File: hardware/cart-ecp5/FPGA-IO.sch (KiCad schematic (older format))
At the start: 9 parts, among them J1 JTAG, U1 LFE5U-25F-xBG256x, U2 W25Q512JVEIM, X1 XO_Generic_NC

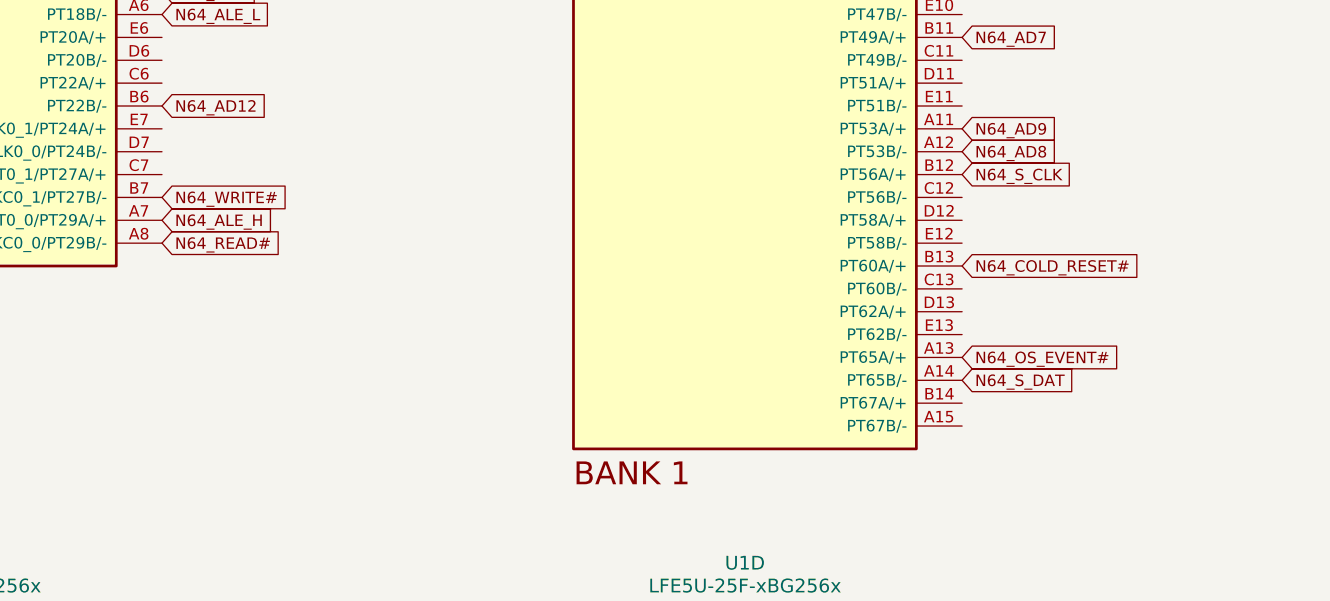
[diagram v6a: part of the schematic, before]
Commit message: Fanout MicroSD and N64 interfaces on the top layer
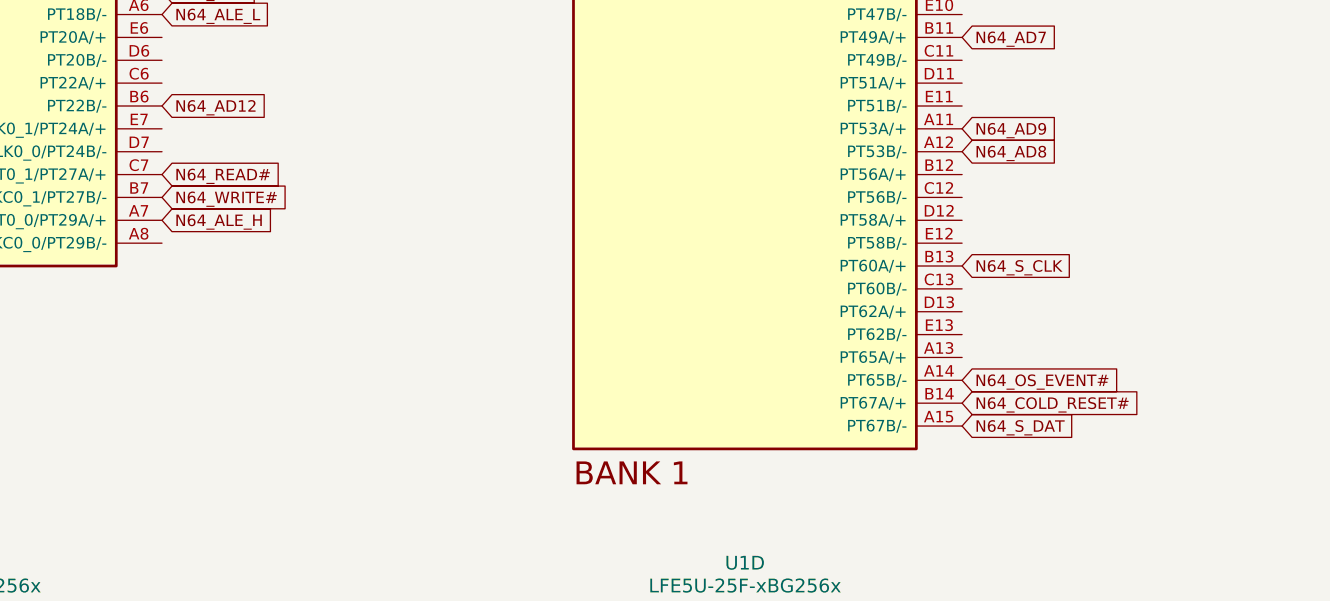
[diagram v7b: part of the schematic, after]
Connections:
- net N64_COLD_RESET#: now also U1.B14 (PT67A/+); no longer U1.B13 (PT60A/+)
- net N64_OS_EVENT#: now also U1.A14 (PT65B/-); no longer U1.A13 (PT65A/+)
- net N64_READ#: now also U1.C7 (PCLKT0_1/PT27A/+); no longer U1.A8 (PCLKC0_0/PT29B/-)
- net N64_S_CLK: now also U1.B13 (PT60A/+); no longer U1.B12 (PT56A/+)
- net N64_S_DAT: now also U1.A15 (PT67B/-); no longer U1.A14 (PT65B/-)
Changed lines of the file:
@@
 Text GLabel 3200 3800 2    50   Input ~ 0
 N64_ALE_H
-Text GLabel 3200 3900 2    50   Input ~ 0
+Text GLabel 3200 3600 2    50   Input ~ 0
 N64_READ#
 Text GLabel 6700 2600 2    50   Input ~ 0
@@
 Text GLabel 6700 3500 2    50   Input ~ 0
 N64_AD8
-Text GLabel 6700 3600 2    50   Input ~ 0
+Text GLabel 6700 4000 2    50   Input ~ 0
 N64_S_CLK
-Text GLabel 6700 4400 2    50   Input ~ 0
+Text GLabel 6700 4500 2    50   Input ~ 0
 N64_OS_EVENT#
-Text GLabel 6700 4000 2    50   Input ~ 0
+Text GLabel 6700 4600 2    50   Input ~ 0
 N64_COLD_RESET#
-Text GLabel 6700 4500 2    50   Input ~ 0
+Text GLabel 6700 4700 2    50   Input ~ 0
 N64_S_DAT
 $Comp

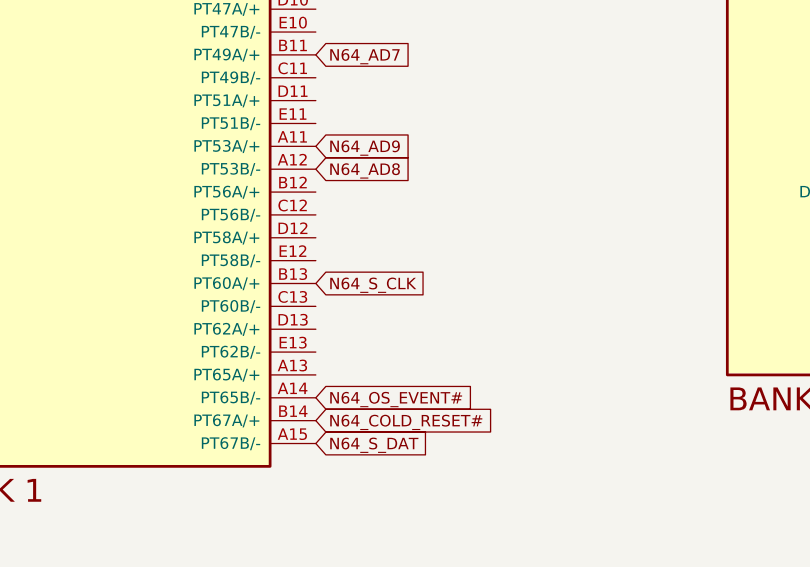
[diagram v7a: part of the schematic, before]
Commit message: Assign FPGA IO for N64_CIC_DATA[12] and add series termination
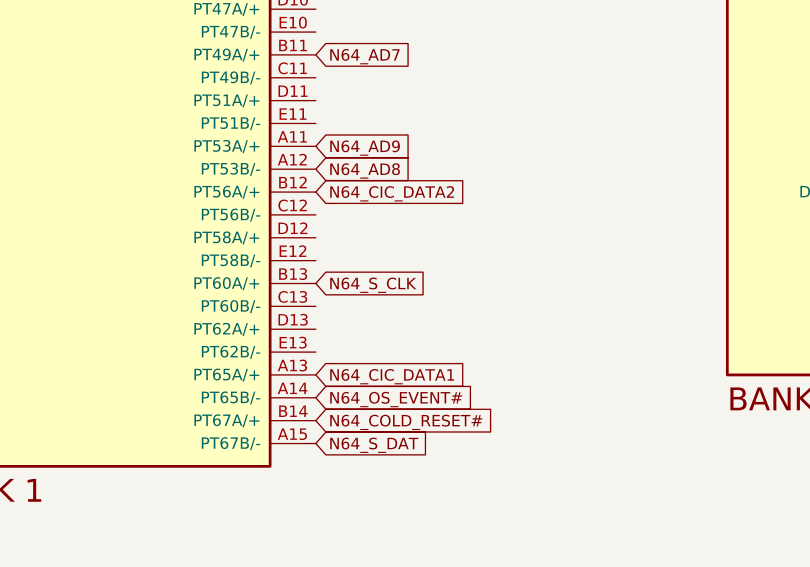
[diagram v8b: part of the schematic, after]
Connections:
- net N64_CIC_DATA1: now reaches U1.A13 (PT65A/+)
- net N64_CIC_DATA2: now reaches U1.B12 (PT56A/+)
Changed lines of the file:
@@
 Text Notes 5150 9750 0    50   ~ 0
 NB. Must assign IO for USB_DET signal
+Text GLabel 6700 4400 2    50   Input ~ 0
+N64_CIC_DATA1
+Text GLabel 6700 3600 2    50   Input ~ 0
+N64_CIC_DATA2
 $EndSCHEMATC
